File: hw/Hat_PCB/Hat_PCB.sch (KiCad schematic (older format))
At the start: 73 parts, among them J1 EE_WP, J10 AudioJack3, J11 AudioJack3_Ground, J2 40HAT, J3 AVR-ISP-6, J4 ID_I2C, J5 RPi_Power, J6 AUD_IN, J7 OUT_SPK_L, J8 OUT_SPK_R, J9 CAP_TOUCH, Q1 DMMT5401, Q2 DMG2305UX, U1 CAT24C32, U2 ATtiny87-MU, U3 NCP1117-3.3_SOT223, U4 TSL2591, U5 BME680, U6 DS3231M, U7 TPA2016D2RTJR

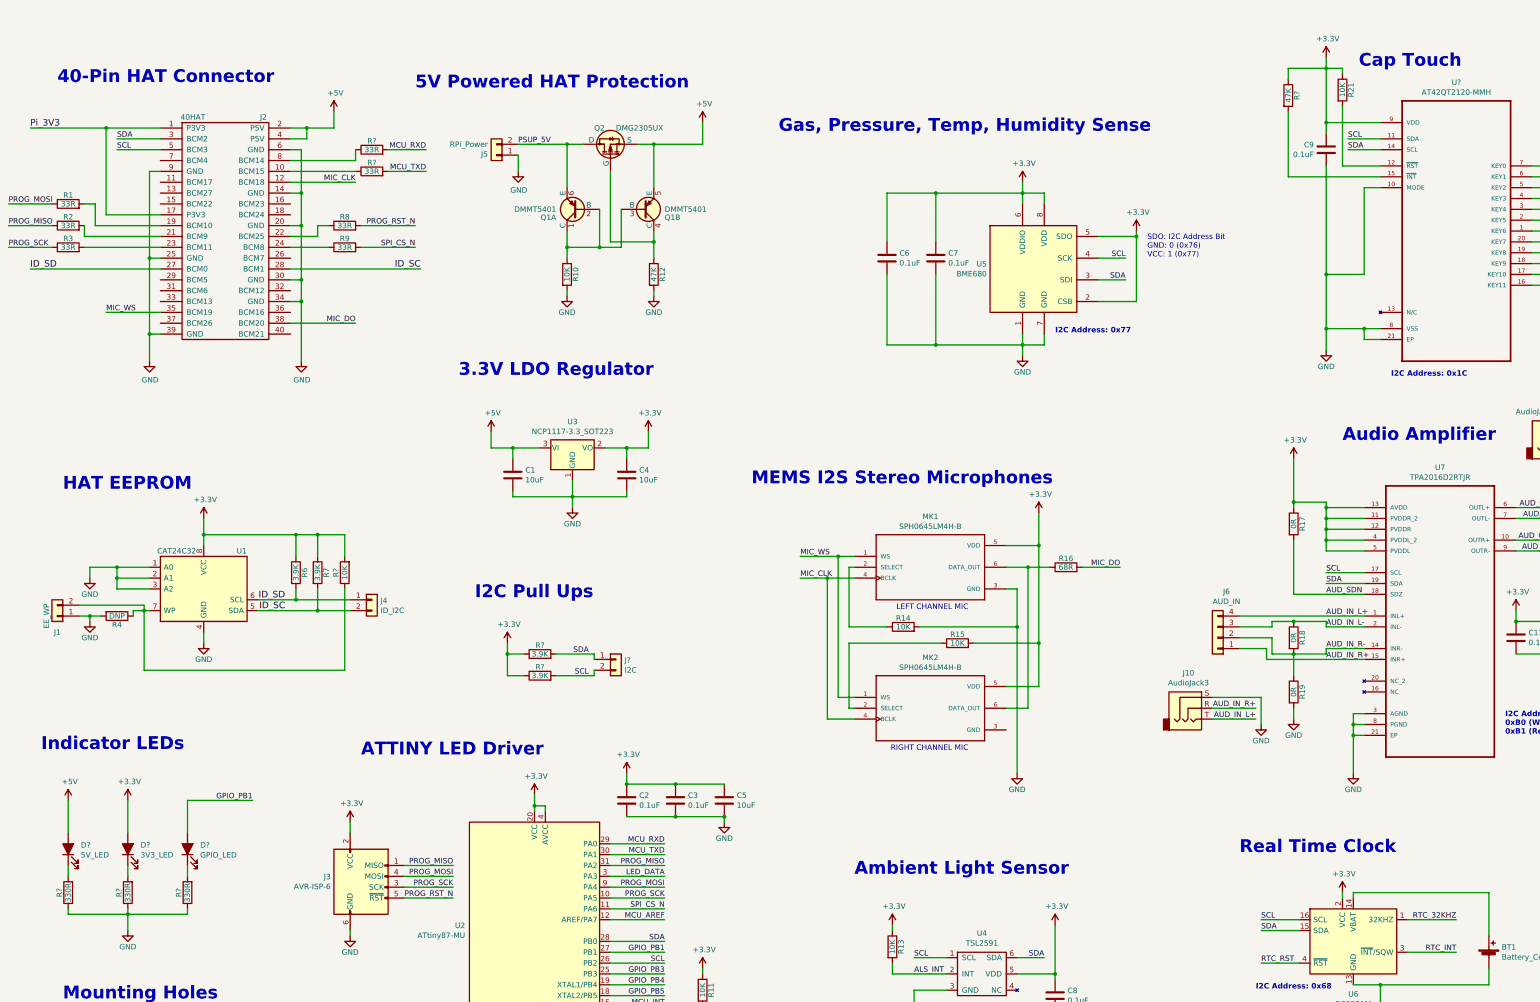
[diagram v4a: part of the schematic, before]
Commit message: change back RTC, finish placement mostly
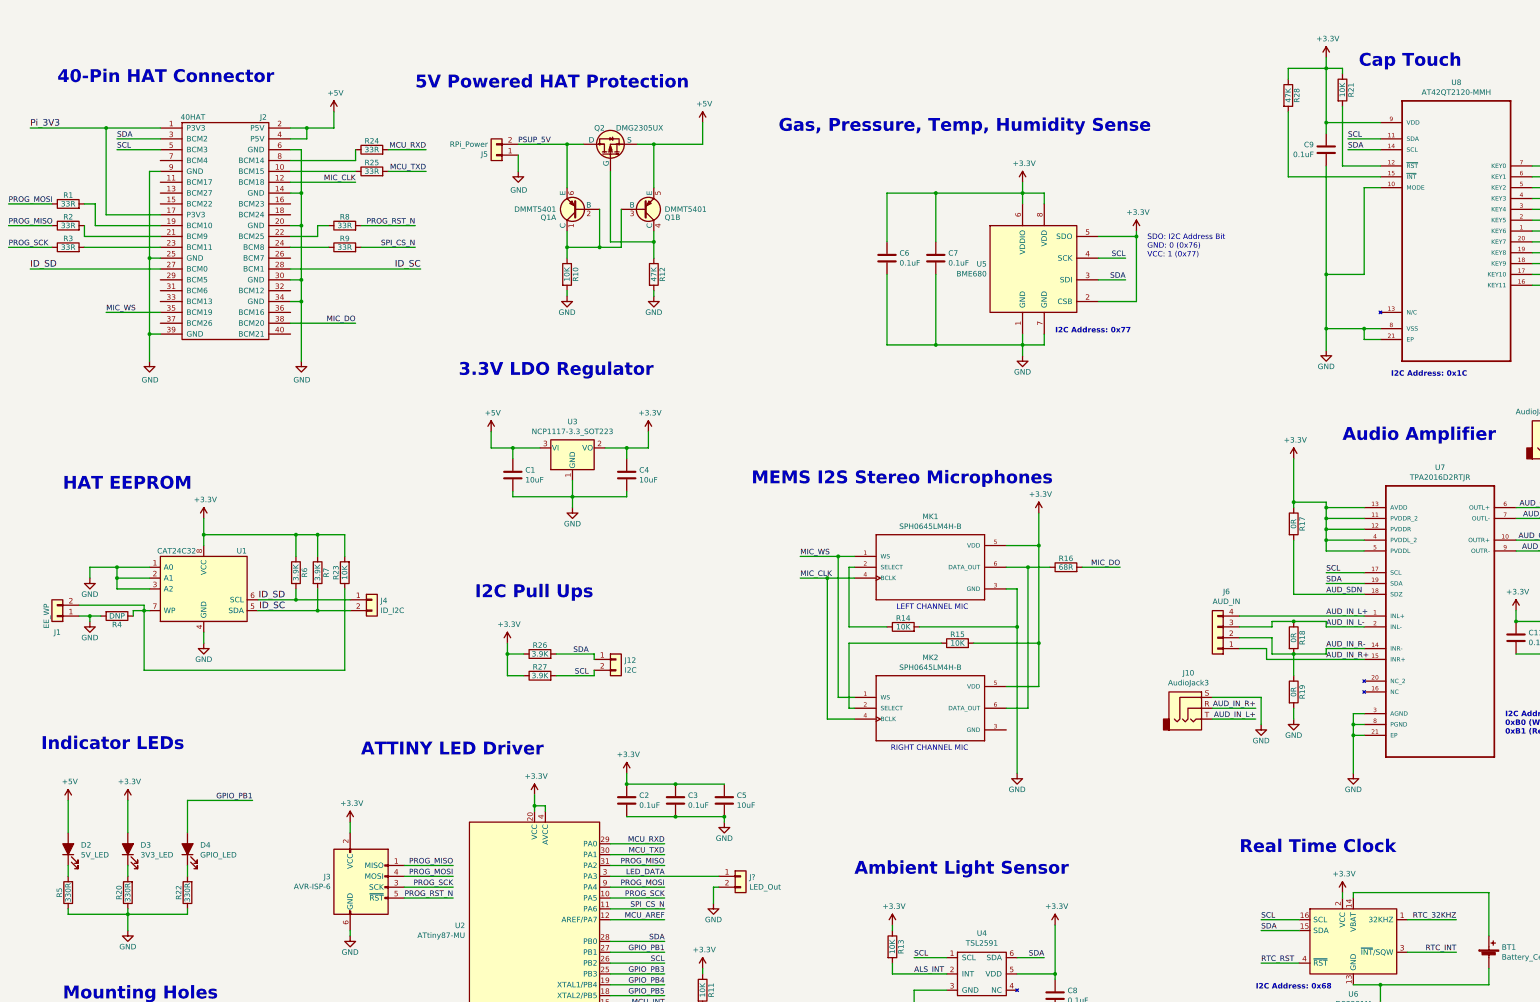
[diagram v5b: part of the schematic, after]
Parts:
- added J?: LED_Out, TerminalBlock_Phoenix:TerminalBlock_Phoenix_MPT-0,5-2-2.54_1x02_P2.54mm_Horizontal, symbol Connector_Generic:Conn_01x02
- D2, D3, D4: renamed from D?; footprint (none) -> Diode_SMD:D_0805_2012Metric_Pad1.15x1.40mm_HandSolder
- J5: footprint Connector_PinHeader_2.54mm:PinHeader_1x02_P2.54mm_Vertical -> TerminalBlock_Phoenix:TerminalBlock_Phoenix_MPT-0,5-2-2.54_1x02_P2.54mm_Horizontal
- gave numbers to parts that had none: 11
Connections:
- net GND: now also J?.2 (Pin_2)
- net LED_DATA: now also J?.1 (Pin_1)
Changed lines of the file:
@@
 F 0 "J5" H 5230 1842 50  0000 L CNN
 F 1 "RPi_Power" H 5230 1751 50  0000 L CNN
-F 2 "Connector_PinHeader_2.54mm:PinHeader_1x02_P2.54mm_Vertical" H 5150 1850 50  0001 C CNN
+F 2 "TerminalBlock_Phoenix:TerminalBlock_Phoenix_MPT-0,5-2-2.54_1x02_P2.54mm_Horizontal" H 5150 1850 50  0001 C CNN
 F 3 "~" H 5150 1850 50  0001 C CNN
 	1    5150 1850
@@
 Text Label 6700 9700 2    50   ~ 0
 MCU_INT
-Wire Wire Line
-	6200 8500 6700 8500
 Text Label 6700 8500 2    50   ~ 0
 LED_DATA
@@
 PROG_RST_N
 $Comp
-L Timer_RTC:DS3231M U6
-U 1 1 5C5E5A43
-P 13050 9100
-F 0 "U6" H 13050 8614 50  0000 C CNN
-F 1 "DS3231M" H 13050 8523 50  0000 C CNN
-F 2 "Package_SO:SOIC-16W_7.5x10.3mm_P1.27mm" H 13050 8500 50  0001 C CNN
-F 3 "http://datasheets.maximintegrated.com/en/ds/DS3231.pdf" H 13320 9150 50  0001 C CNN
-	1    13050 9100
-	1    0    0    -1
-$EndComp
-$Comp
 L power:GND #PWR0138
 U 1 1 5C6141F2
@@
 $EndComp
 Wire Wire Line
-	12950 8700 12950 8650
-Wire Wire Line
 	12550 8900 12200 8900
 Wire Wire Line
@@
 Text Label 12200 9000 0    50   ~ 0
 SDA
-Wire Wire Line
-	12200 9300 12550 9300
-Text Label 12200 9300 0    50   ~ 0
-RTC_RST
 Text Label 14000 8900 2    50   ~ 0
 RTC_32KHZ
@@
 RTC_INT
 Wire Wire Line
-	13050 9500 13300 9500
-Wire Wire Line
-	13300 9500 13300 9650
-Wire Wire Line
-	13050 8700 13050 8650
-Wire Wire Line
 	14300 8650 14300 9050
-Wire Wire Line
-	13050 8650 14300 8650
 $Comp
 L Device:Battery_Cell BT1
@@
 Wire Wire Line
 	14300 9350 14300 9500
-Wire Wire Line
-	14300 9500 13300 9500
-Connection ~ 13300 9500
 $Comp
 L BAV99:BAV99 D1
@@
 To do:\n- Better connectors\n- Double check reference schematics for possible missing parts\n- Placement for passives
 $Comp
-L Device:LED_ALT D?
+L Device:LED_ALT D2
 U 1 1 5CCDA4F1
 P 1200 8250
-F 0 "D?" V 1238 8133 50  0000 R CNN
+F 0 "D2" V 1238 8133 50  0000 R CNN
 F 1 "5V_LED" V 1147 8133 50  0000 R CNN
-F 2 "" H 1200 8250 50  0001 C CNN
+F 2 "Diode_SMD:D_0805_2012Metric_Pad1.15x1.40mm_HandSolder" H 1200 8250 50  0001 C CNN
 F 3 "~" H 1200 8250 50  0001 C CNN
 	1    1200 8250
@@
 $EndComp
 $Comp
-L Device:LED_ALT D?
+L Device:LED_ALT D3
 U 1 1 5CCDB72A
 P 1750 8250
-F 0 "D?" V 1788 8133 50  0000 R CNN
+F 0 "D3" V 1788 8133 50  0000 R CNN
 F 1 "3V3_LED" V 1697 8133 50  0000 R CNN
-F 2 "" H 1750 8250 50  0001 C CNN
+F 2 "Diode_SMD:D_0805_2012Metric_Pad1.15x1.40mm_HandSolder" H 1750 8250 50  0001 C CNN
 F 3 "~" H 1750 8250 50  0001 C CNN
 	1    1750 8250
@@
 $EndComp
 $Comp
-L Device:LED_ALT D?
+L Device:LED_ALT D4
 U 1 1 5CCF5129
 P 2300 8250
-F 0 "D?" V 2338 8133 50  0000 R CNN
+F 0 "D4" V 2338 8133 50  0000 R CNN
 F 1 "GPIO_LED" V 2247 8133 50  0000 R CNN
-F 2 "" H 2300 8250 50  0001 C CNN
+F 2 "Diode_SMD:D_0805_2012Metric_Pad1.15x1.40mm_HandSolder" H 2300 8250 50  0001 C CNN
 F 3 "~" H 2300 8250 50  0001 C CNN
 	1    2300 8250
@@
 	1200 8400 1200 8500
 $Comp
-L Device:R R?
+L Device:R R5
 U 1 1 5CDAC7B2
 P 1200 8650
-F 0 "R?" V 1280 8650 50  0000 C CNN
+F 0 "R5" V 1280 8650 50  0000 C CNN
 F 1 "330R" V 1200 8650 50  0000 C CNN
 F 2 "Resistor_SMD:R_0603_1608Metric_Pad1.05x0.95mm_HandSolder" V 1130 8650 50  0001 C CNN
@@
 $EndComp
 $Comp
-L Device:R R?
+L Device:R R20
 U 1 1 5CDC730F
 P 1750 8650
-F 0 "R?" V 1830 8650 50  0000 C CNN
+F 0 "R20" V 1830 8650 50  0000 C CNN
 F 1 "330R" V 1750 8650 50  0000 C CNN
 F 2 "Resistor_SMD:R_0603_1608Metric_Pad1.05x0.95mm_HandSolder" V 1680 8650 50  0001 C CNN
@@
 $EndComp
 $Comp
-L Device:R R?
+L Device:R R22
 U 1 1 5CDE1E65
 P 2300 8650
-F 0 "R?" V 2380 8650 50  0000 C CNN
+F 0 "R22" V 2380 8650 50  0000 C CNN
 F 1 "330R" V 2300 8650 50  0000 C CNN
 F 2 "Resistor_SMD:R_0603_1608Metric_Pad1.05x0.95mm_HandSolder" V 2230 8650 50  0001 C CNN
@@
 $EndComp
 $Comp
-L power:+5V #PWR?
+L power:+5V #PWR0115
 U 1 1 5CDFD400
 P 1200 7800
-F 0 "#PWR?" H 1200 7650 50  0001 C CNN
+F 0 "#PWR0115" H 1200 7650 50  0001 C CNN
 F 1 "+5V" H 1215 7973 50  0000 C CNN
 F 2 "" H 1200 7800 50  0001 C CNN
@@
 $EndComp
 $Comp
-L power:+3.3V #PWR?
+L power:+3.3V #PWR0143
 U 1 1 5CE18419
 P 1750 7800
-F 0 "#PWR?" H 1750 7650 50  0001 C CNN
+F 0 "#PWR0143" H 1750 7650 50  0001 C CNN
 F 1 "+3.3V" H 1765 7973 50  0000 C CNN
 F 2 "" H 1750 7800 50  0001 C CNN
@@
 	2300 8850 1750 8850
 $Comp
-L power:GND #PWR?
+L power:GND #PWR0144
 U 1 1 5CEA2CC6
 P 1750 9000
-F 0 "#PWR?" H 1750 8750 50  0001 C CNN
+F 0 "#PWR0144" H 1750 8750 50  0001 C CNN
 F 1 "GND" H 1750 8850 50  0000 C CNN
 F 2 "" H 1750 9000 50  0000 C CNN
@@
 Connection ~ 5250 6450
 $Comp
-L power:+3.3V #PWR?
+L power:+3.3V #PWR0145
 U 1 1 5CF70227
 P 5250 6350
-F 0 "#PWR?" H 5250 6200 50  0001 C CNN
+F 0 "#PWR0145" H 5250 6200 50  0001 C CNN
 F 1 "+3.3V" H 5265 6523 50  0000 C CNN
 F 2 "" H 5250 6350 50  0001 C CNN
@@
 $EndComp
 $Comp
-L Device:R R?
+L Device:R R27
 U 1 1 5CF8E09B
 P 5550 6650
-F 0 "R?" V 5630 6650 50  0000 C CNN
+F 0 "R27" V 5630 6650 50  0000 C CNN
 F 1 "3.9K" V 5550 6650 50  0000 C CNN
 F 2 "Resistor_SMD:R_0603_1608Metric_Pad1.05x0.95mm_HandSolder" V 5480 6650 50  0001 C CNN
@@
 $EndComp
 $Comp
-L Device:R R?
+L Device:R R26
 U 1 1 5CF8E0A2
 P 5550 6450
-F 0 "R?" V 5630 6450 50  0000 C CNN
+F 0 "R26" V 5630 6450 50  0000 C CNN
 F 1 "3.9K" V 5550 6450 50  0000 C CNN
 F 2 "Resistor_SMD:R_0603_1608Metric_Pad1.05x0.95mm_HandSolder" V 5480 6450 50  0001 C CNN
@@
 I2C Pull Ups
 $Comp
-L Connector_Generic:Conn_01x02 J?
+L Connector_Generic:Conn_01x02 J12
 U 1 1 5D14A080
 P 6250 6500
-F 0 "J?" H 6330 6492 50  0000 L CNN
+F 0 "J12" H 6330 6492 50  0000 L CNN
 F 1 "I2C" H 6330 6401 50  0000 L CNN
 F 2 "Connector_PinHeader_2.54mm:PinHeader_1x02_P2.54mm_Vertical" H 6250 6500 50  0001 C CNN
@@
 	5700 6650 6050 6650
 $Comp
-L Device:R R?
+L Device:R R23
 U 1 1 5D1A5756
 P 3750 5700
-F 0 "R?" V 3830 5700 50  0000 C CNN
+F 0 "R23" V 3830 5700 50  0000 C CNN
 F 1 "10K" V 3750 5700 50  0000 C CNN
 F 2 "Resistor_SMD:R_0603_1608Metric_Pad1.05x0.95mm_HandSolder" V 3680 5700 50  0001 C CNN
@@
 	3250 2000 3850 2000
 $Comp
-L Device:R R?
+L Device:R R24
 U 1 1 5D279A5D
 P 4000 1800
-F 0 "R?" V 4080 1800 50  0000 C CNN
+F 0 "R24" V 4080 1800 50  0000 C CNN
 F 1 "33R" V 4000 1800 50  0000 C CNN
 F 2 "Resistor_SMD:R_0603_1608Metric_Pad1.05x0.95mm_HandSolder" V 3930 1800 50  0001 C CNN
@@
 $EndComp
 $Comp
-L Device:R R?
+L Device:R R25
 U 1 1 5D279A64
 P 4000 2000
-F 0 "R?" V 4080 2000 50  0000 C CNN
+F 0 "R25" V 4080 2000 50  0000 C CNN
 F 1 "33R" V 4000 2000 50  0000 C CNN
 F 2 "Resistor_SMD:R_0603_1608Metric_Pad1.05x0.95mm_HandSolder" V 3930 2000 50  0001 C CNN
@@
 	4150 1800 4500 1800
 $Comp
-L AT42QT2120-MMH:AT42QT2120-MMH U?
+L AT42QT2120-MMH:AT42QT2120-MMH U8
 U 1 1 5D3991AC
 P 14000 2450
-F 0 "U?" H 14000 3720 50  0000 C CNN
+F 0 "U8" H 14000 3720 50  0000 C CNN
 F 1 "AT42QT2120-MMH" H 14000 3629 50  0000 C CNN
 F 2 "QFN45P300X300X85-21N" H 14000 2450 50  0001 L BNN
@@
 	12450 2050 12450 1450
 $Comp
-L Device:R R?
+L Device:R R28
 U 1 1 5D5B4921
 P 12450 1300
-F 0 "R?" V 12530 1300 50  0000 C CNN
+F 0 "R28" V 12530 1300 50  0000 C CNN
 F 1 "47K" V 12450 1300 50  0000 C CNN
 F 2 "Resistor_SMD:R_0603_1608Metric_Pad1.05x0.95mm_HandSolder" V 12380 1300 50  0001 C CNN
@@
 Wire Wire Line
 	13150 3450 12800 3450
+Wire Wire Line
+	13300 9500 13300 9650
+Wire Wire Line
+	12950 8700 12950 8650
+Text Label 12200 9300 0    50   ~ 0
+RTC_RST
+Wire Wire Line
+	12200 9300 12550 9300
+Wire Wire Line
+	13050 9500 13300 9500
+Connection ~ 13300 9500
+Wire Wire Line
+	14300 9500 13300 9500
+Wire Wire Line
+	13050 8650 14300 8650
+Wire Wire Line
+	13050 8700 13050 8650
+$Comp
+L Timer_RTC:DS3231M U6
+U 1 1 5C5E5A43
+P 13050 9100
+F 0 "U6" H 13050 8614 50  0000 C CNN
+F 1 "DS3231M" H 13050 8523 50  0000 C CNN
+F 2 "Package_SO:SOIC-16W_7.5x10.3mm_P1.27mm" H 13050 8500 50  0001 C CNN
+F 3 "http://datasheets.maximintegrated.com/en/ds/DS3231.pdf" H 13320 9150 50  0001 C CNN
+	1    13050 9100
+	1    0    0    -1
+$EndComp
+$Comp
+L Connector_Generic:Conn_01x02 J?
+U 1 1 5DA18A45
+P 7400 8500
+F 0 "J?" H 7480 8492 50  0000 L CNN
+F 1 "LED_Out" H 7480 8401 50  0000 L CNN
+F 2 "TerminalBlock_Phoenix:TerminalBlock_Phoenix_MPT-0,5-2-2.54_1x02_P2.54mm_Horizontal" H 7400 8500 50  0001 C CNN
+F 3 "~" H 7400 8500 50  0001 C CNN
+	1    7400 8500
+	1    0    0    -1
+$EndComp
+$Comp
+L power:GND #PWR?
+U 1 1 5DA94BD7
+P 7150 8750
+F 0 "#PWR?" H 7150 8500 50  0001 C CNN
+F 1 "GND" H 7150 8600 50  0000 C CNN
+F 2 "" H 7150 8750 50  0000 C CNN
+F 3 "" H 7150 8750 50  0000 C CNN
+	1    7150 8750
+	1    0    0    -1
+$EndComp
+Wire Wire Line
+	7150 8750 7150 8600
+Wire Wire Line
+	7150 8600 7200 8600
+Wire Wire Line
+	6200 8500 7200 8500
 $EndSCHEMATC
